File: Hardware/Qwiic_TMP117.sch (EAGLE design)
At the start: 26 parts, among them J1 PTH, U1 TMP117

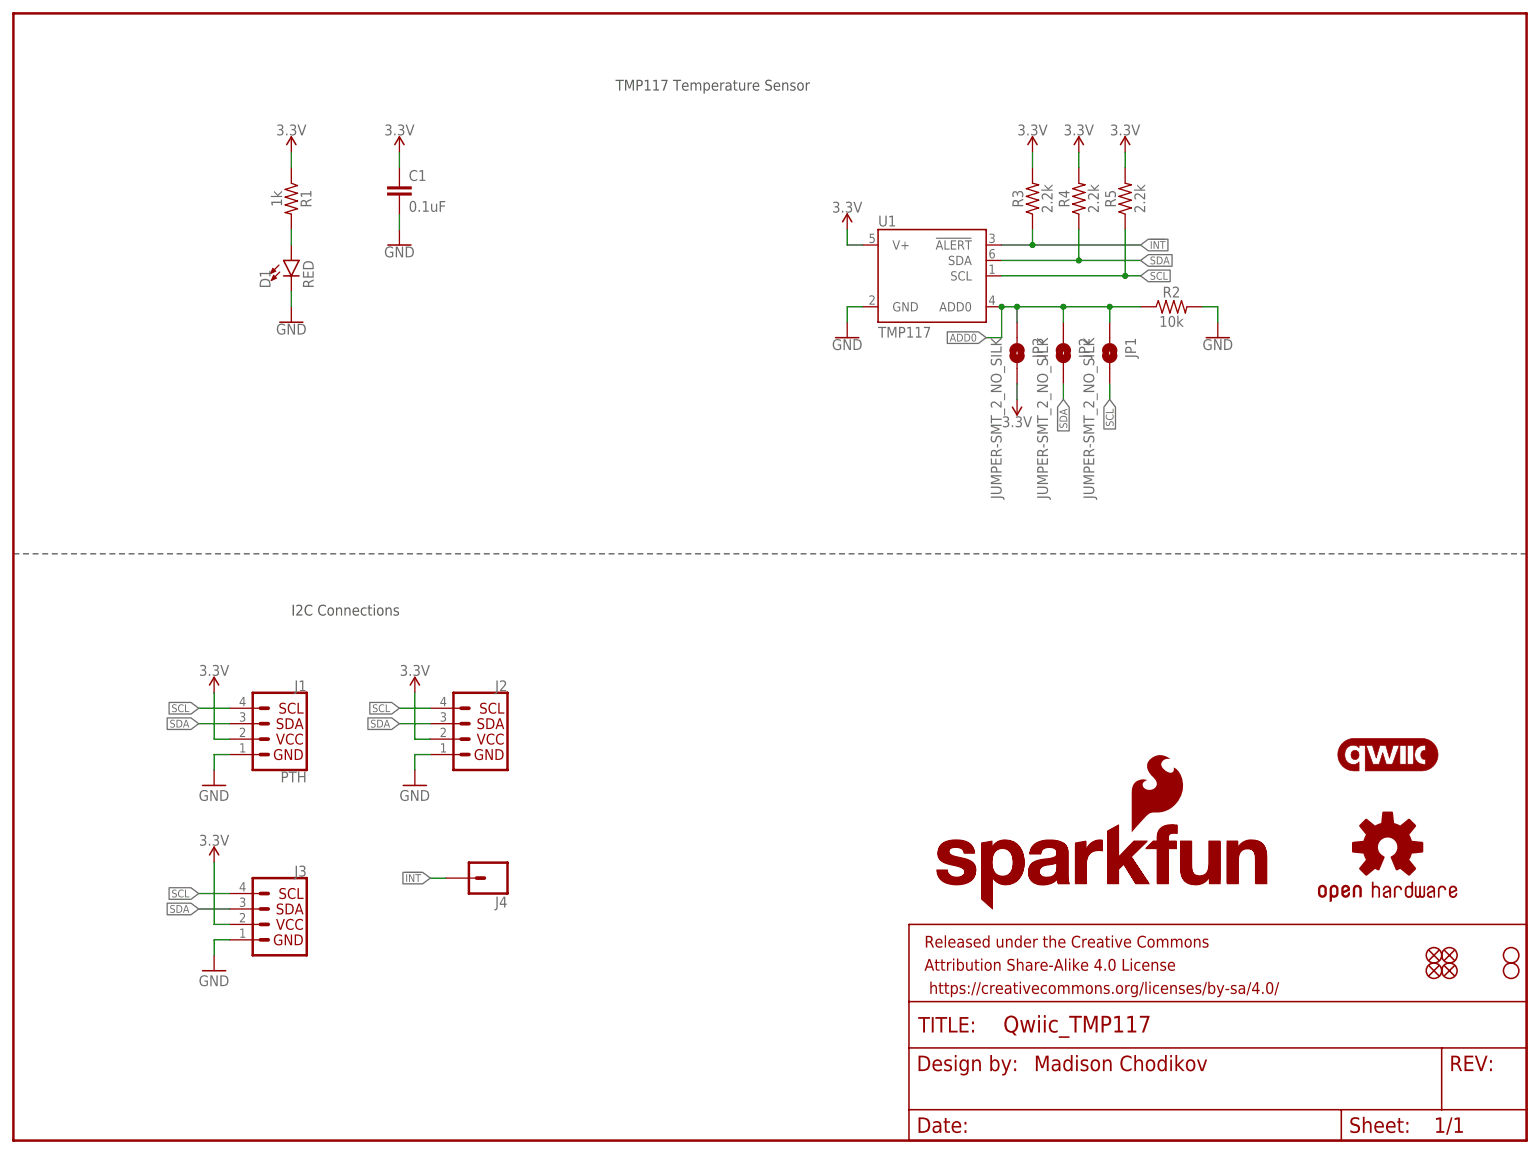
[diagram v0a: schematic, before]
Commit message: Updated Schematic and Boar
Fixed the board with the polygon and added a table to the schematic describing the pin addresses for ADD0
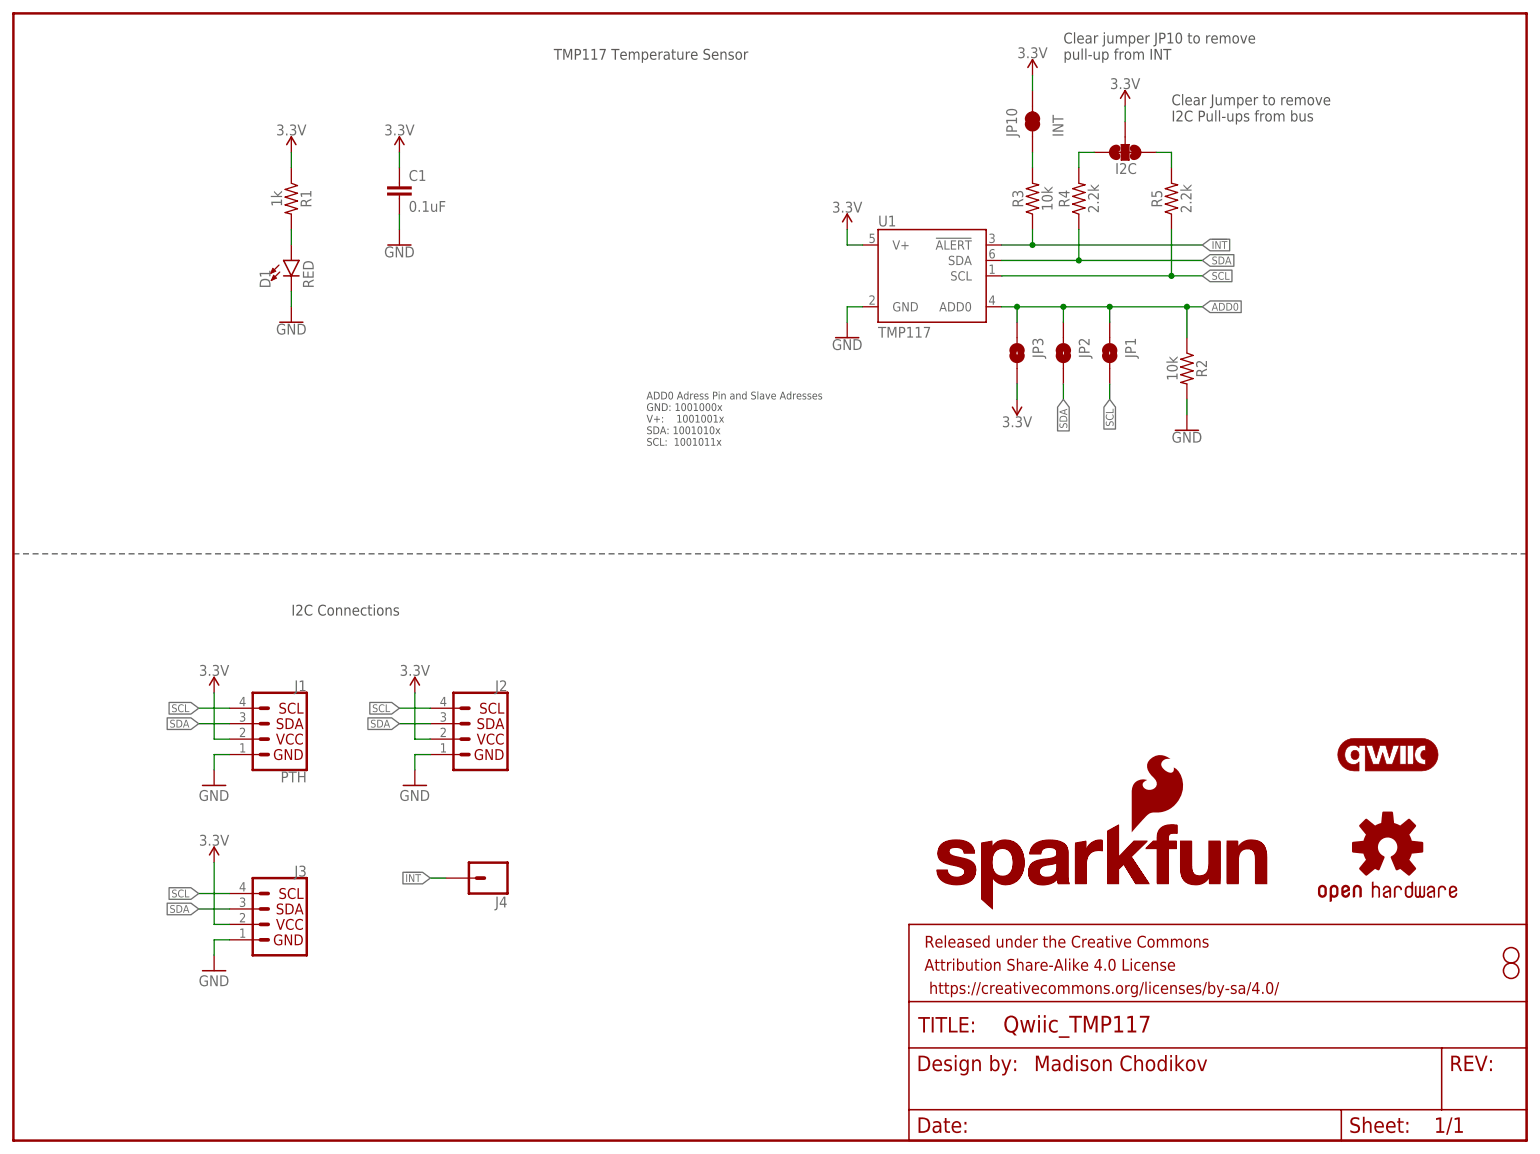
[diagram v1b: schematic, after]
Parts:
- removed JP4, JP5, JP6, JP7: FIDUCIALUFIDUCIAL, SparkFun:FIDUCIALUFIDUCIAL
- added I2C: JUMPER-SMT_3_2-NC_TRACE_SILK, SparkFun-Jumpers:JUMPER-SMT_3_2-NC_TRACE_SILK
- added JP10: INT, SparkFun-Passives:JUMPER-PAD-2-NC_BY_TRACE
- R3: value 2.2k -> 10k; device SparkFun-Resistors:2.2KOHM-0603-1/10W-1% -> SparkFun-Resistors:10KOHM-0603-1/10W-1%
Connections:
- new net N$2: I2C.1, R5.2
- new net N$3: I2C.3, R4.2
- new net N$4: JP10.1, R3.2
- net 3.3V: now also I2C.2, JP10.2; no longer R3.2, R4.2, R5.2
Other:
- note added: "ADD0 Adress Pin and Slave Adresses GND: 1001000x V+: 1001001x SDA: 1001010x SCL: 1001011x"
- note added: "Clear Jumper to remove I2C Pull-ups from bus"
- note added: "Clear jumper JP10 to remove pull-up from INT"
- moved on the sheet: R2, R5

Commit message: Updated PCB
Fixed the board to meet the specifications for the data sheet's PCB considerations
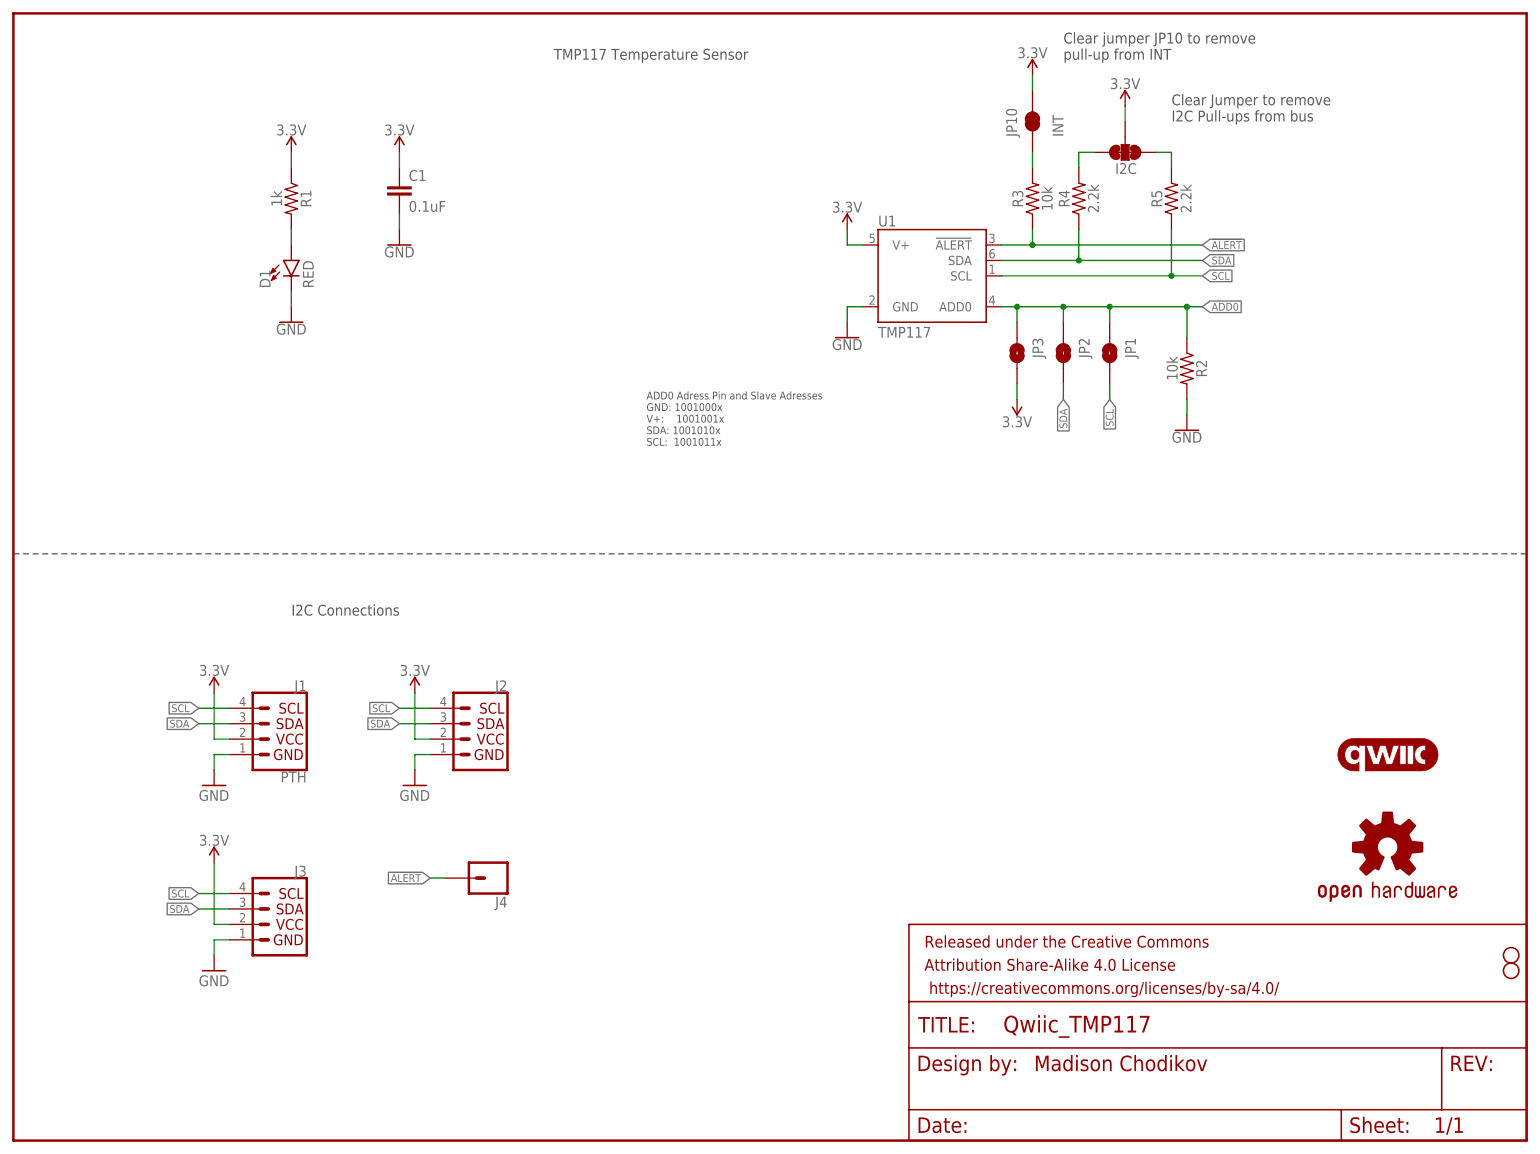
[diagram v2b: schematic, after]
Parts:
- removed U$1: SFE_LOGO_NAME.1_INCH, SparkFun-Aesthetics:SFE_LOGO_NAME.1_INCH
- removed U$2: SFE_LOGO_NAME_FLAME.1_INCH, SparkFun-Aesthetics:SFE_LOGO_NAME_FLAME.1_INCH
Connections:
- net !INT renamed !ALERT
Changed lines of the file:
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@@
 <part name="J4" library="SparkFun-Connectors" deviceset="CONN_01" device="PTH_NO_SILK_YES_STOP"/>
 <part name="SUPPLY2" library="SparkFun-PowerSymbols" library_urn="urn:adsk.eagle:library:530" deviceset="3.3V" device=""/>
-<part name="U$2" library="SparkFun-Aesthetics" deviceset="SFE_LOGO_NAME_FLAME" device=".1_INCH"/>
 <part name="LOGO1" library="SparkFun-Aesthetics" deviceset="OSHW-LOGO" device="MINI"/>
 <part name="SUPPLY7" library="SparkFun-PowerSymbols" deviceset="3.3V" device=""/>
@@
 <part name="JP8" library="SparkFun" deviceset="STAND-OFF" device=""/>
 <part name="JP9" library="SparkFun" deviceset="STAND-OFF" device=""/>
-<part name="U$1" library="SparkFun-Aesthetics" deviceset="SFE_LOGO_NAME" device=".1_INCH"/>
 <part name="U$3" library="SparkFun-Aesthetics" deviceset="QWIIC_LOGO" device="_4MM"/>
 <part name="I2C" library="SparkFun-Jumpers" library_urn="urn:adsk.eagle:library:528" deviceset="JUMPER-SMT_3_2-NC_TRACE" device="_SILK" package3d_urn="urn:adsk.eagle:package:39289/1" value=""/>
@@
 <attribute name="VALUE" x="165.1" y="119.126" size="1.778" layer="96" rot="R180" align="bottom-center"/>
 </instance>
-<instance part="U$2" gate="G$1" x="151.13" y="37.592" smashed="yes"/>
 <instance part="LOGO1" gate="G$1" x="226.06" y="48.26" smashed="yes"/>
 <instance part="SUPPLY7" gate="G$1" x="66.04" y="73.66" smashed="yes">
@@
 <instance part="JP8" gate="G$1" x="246.38" y="30.48" smashed="yes"/>
 <instance part="JP9" gate="G$1" x="246.38" y="27.94" smashed="yes"/>
-<instance part="U$1" gate="G$1" x="149.86" y="38.1" smashed="yes"/>
 <instance part="U$3" gate="G$1" x="226.06" y="63.5" smashed="yes"/>
 <instance part="I2C" gate="G$1" x="182.88" y="162.56" smashed="yes" rot="R270">
@@
 </segment>
 </net>
-<net name="!INT" class="0">
+<net name="!ALERT" class="0">
 <segment>
 <pinref part="J4" gate="G$1" pin="1"/>
@@
 <pinref part="R3" gate="G$1" pin="1"/>
 <wire x1="162.56" y1="147.32" x2="167.64" y2="147.32" width="0.1524" layer="91"/>
-<label x="195.58" y="147.32" size="1.27" layer="95" xref="yes"/>
 <wire x1="167.64" y1="147.32" x2="195.58" y2="147.32" width="0.1524" layer="91"/>
 <wire x1="167.64" y1="149.86" x2="167.64" y2="147.32" width="0.1524" layer="91"/>
 <junction x="167.64" y="147.32"/>
-</segment>
-</net>
+<label x="195.58" y="147.32" size="1.27" layer="95" xref="yes"/>
+</segment>
+</net>

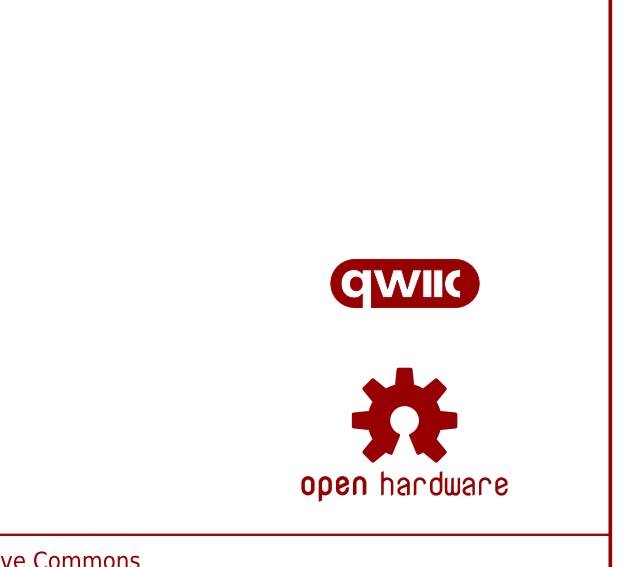
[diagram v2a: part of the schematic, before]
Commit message: Updated Board
Fixed wiring and polygons
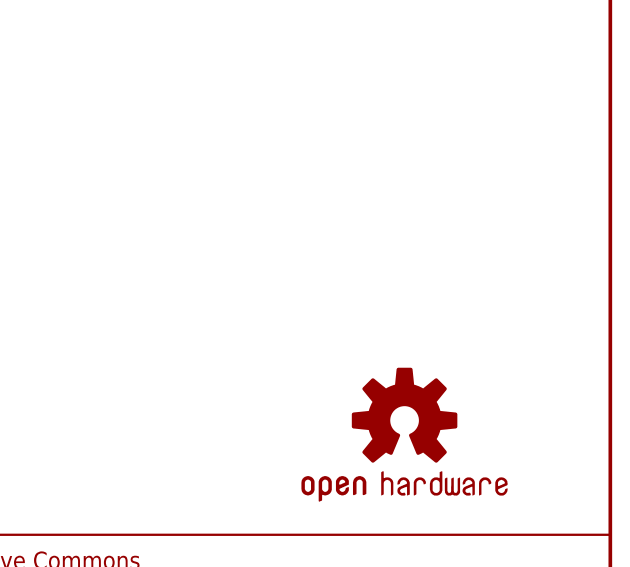
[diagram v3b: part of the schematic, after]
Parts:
- removed U$3: QWIIC_LOGO_4MM, SparkFun-Aesthetics:QWIIC_LOGO_4MM
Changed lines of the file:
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@@
 <part name="JP8" library="SparkFun" deviceset="STAND-OFF" device=""/>
 <part name="JP9" library="SparkFun" deviceset="STAND-OFF" device=""/>
-<part name="U$3" library="SparkFun-Aesthetics" deviceset="QWIIC_LOGO" device="_4MM"/>
 <part name="I2C" library="SparkFun-Jumpers" library_urn="urn:adsk.eagle:library:528" deviceset="JUMPER-SMT_3_2-NC_TRACE" device="_SILK" package3d_urn="urn:adsk.eagle:package:39289/1" value=""/>
 <part name="JP10" library="SparkFun-Passives" deviceset="JUMPER-PAD-2-NC_BY_TRACE" device="" value="INT"/>
@@
 <instance part="JP8" gate="G$1" x="246.38" y="30.48" smashed="yes"/>
 <instance part="JP9" gate="G$1" x="246.38" y="27.94" smashed="yes"/>
-<instance part="U$3" gate="G$1" x="226.06" y="63.5" smashed="yes"/>
 <instance part="I2C" gate="G$1" x="182.88" y="162.56" smashed="yes" rot="R270">
 <attribute name="NAME" x="181.229" y="159.004" size="1.778" layer="95" font="vector"/>

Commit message: Final Design
Final updated board with the production panelized board and Gerber files
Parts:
- removed U1: TMP117, my-library:TMP117
- added U2: TMP117, TMP117:TMP117
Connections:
- removed net !ALERT: J4.1, R3.1, U1.!ALERT
- new net !INT: J4.1, R3.1, U2.!INT
- net 3.3V: now also U2.V+; no longer U1.V+
- net ADD0: now also U2.ADD0; no longer U1.ADD0
- net GND: now also U2.GND; no longer U1.GND
- net SCL: now also U2.SCL; no longer U1.SCL
- net SDA: now also U2.SDA; no longer U1.SDA
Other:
- note added: "ADD0 Adress Pin and Slave Adresses GND: 1001000x V+: 1001001x SDA: 1001010x SCL: 1001011x x represents the read-write bit"
- note removed: "ADD0 Adress Pin and Slave Adresses GND: 1001000x V+: 1001001x SDA: 1001010x SCL: 1001011x"
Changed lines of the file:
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@@
 <part name="GND5" library="SparkFun" deviceset="GND" device=""/>
 <part name="GND6" library="SparkFun" deviceset="GND" device=""/>
-<part name="U1" library="my-library" deviceset="TMP117" device=""/>
 <part name="JP1" library="SparkFun-Jumpers" library_urn="urn:adsk.eagle:library:528" deviceset="JUMPER-SMT_2_NO" device="_SILK" package3d_urn="urn:adsk.eagle:package:39279/1" value=""/>
 <part name="SUPPLY5" library="SparkFun-PowerSymbols" library_urn="urn:adsk.eagle:library:530" deviceset="3.3V" device=""/>
@@
 <part name="I2C" library="SparkFun-Jumpers" library_urn="urn:adsk.eagle:library:528" deviceset="JUMPER-SMT_3_2-NC_TRACE" device="_SILK" package3d_urn="urn:adsk.eagle:package:39289/1" value=""/>
 <part name="JP10" library="SparkFun-Passives" deviceset="JUMPER-PAD-2-NC_BY_TRACE" device="" value="INT"/>
+<part name="U2" library="TMP117" deviceset="TMP117" device=""/>
 </parts>
 <sheets>
@@
 V+:    1001001x
 SDA: 1001010x
-SCL:  1001011x</text>
+SCL:  1001011x
+x represents the read-write bit</text>
 </plain>
 <instances>
@@
 <attribute name="VALUE" x="30.48" y="25.4" size="1.778" layer="96"/>
 </instance>
-<instance part="U1" gate="G$1" x="149.86" y="142.24" smashed="yes">
-<attribute name="NAME" x="142.24" y="150.368" size="1.778" layer="95"/>
-<attribute name="VALUE" x="142.24" y="132.08" size="1.778" layer="96"/>
-</instance>
 <instance part="JP1" gate="G$1" x="180.34" y="129.54" smashed="yes" rot="R270">
 <attribute name="NAME" x="182.88" y="132.08" size="1.778" layer="95" font="vector" rot="R270"/>
@@
 <attribute name="VALUE" x="172.72" y="165.1" size="1.778" layer="96" rot="R90"/>
 </instance>
+<instance part="U2" gate="G$1" x="149.86" y="142.24" smashed="yes">
+<attribute name="NAME" x="142.24" y="150.368" size="1.778" layer="95"/>
+<attribute name="VALUE" x="137.16" y="132.08" size="1.778" layer="96"/>
+</instance>
 </instances>
 <busses>
@@
 <segment>
 <pinref part="GND2" gate="1" pin="GND"/>
-<pinref part="U1" gate="G$1" pin="GND"/>
 <wire x1="137.16" y1="134.62" x2="137.16" y2="137.16" width="0.1524" layer="91"/>
 <wire x1="137.16" y1="137.16" x2="139.7" y2="137.16" width="0.1524" layer="91"/>
+<pinref part="U2" gate="G$1" pin="GND"/>
 </segment>
 <segment>
@@
 <pinref part="SUPPLY6" gate="G$1" pin="3.3V"/>
 <wire x1="137.16" y1="149.86" x2="137.16" y2="147.32" width="0.1524" layer="91"/>
-<pinref part="U1" gate="G$1" pin="V+"/>
 <wire x1="137.16" y1="147.32" x2="139.7" y2="147.32" width="0.1524" layer="91"/>
+<pinref part="U2" gate="G$1" pin="V+"/>
 </segment>
 <segment>
@@
 </segment>
 <segment>
-<pinref part="U1" gate="G$1" pin="SDA"/>
 <pinref part="R4" gate="G$1" pin="1"/>
 <wire x1="175.26" y1="144.78" x2="162.56" y2="144.78" width="0.1524" layer="91"/>
@@
 <junction x="175.26" y="144.78"/>
 <label x="195.58" y="144.78" size="1.27" layer="95" xref="yes"/>
+<pinref part="U2" gate="G$1" pin="SDA"/>
 </segment>
 <segment>
@@
 </segment>
 <segment>
-<pinref part="U1" gate="G$1" pin="SCL"/>
 <pinref part="R5" gate="G$1" pin="1"/>
 <wire x1="190.5" y1="142.24" x2="162.56" y2="142.24" width="0.1524" layer="91"/>
@@
 <junction x="190.5" y="142.24"/>
 <label x="195.58" y="142.24" size="1.27" layer="95" xref="yes"/>
+<pinref part="U2" gate="G$1" pin="SCL"/>
 </segment>
 <segment>
@@
 </segment>
 </net>
-<net name="!ALERT" class="0">
+<net name="!INT" class="0">
 <segment>
 <pinref part="J4" gate="G$1" pin="1"/>
@@
 </segment>
 <segment>
-<pinref part="U1" gate="G$1" pin="!ALERT"/>
 <pinref part="R3" gate="G$1" pin="1"/>
 <wire x1="162.56" y1="147.32" x2="167.64" y2="147.32" width="0.1524" layer="91"/>
 <wire x1="167.64" y1="147.32" x2="195.58" y2="147.32" width="0.1524" layer="91"/>
+<label x="195.58" y="147.32" size="1.27" layer="95" xref="yes"/>
+<pinref part="U2" gate="G$1" pin="!INT"/>
 <wire x1="167.64" y1="149.86" x2="167.64" y2="147.32" width="0.1524" layer="91"/>
 <junction x="167.64" y="147.32"/>
-<label x="195.58" y="147.32" size="1.27" layer="95" xref="yes"/>
 </segment>
 </net>
@@
 <net name="ADD0" class="0">
 <segment>
-<pinref part="U1" gate="G$1" pin="ADD0"/>
 <wire x1="162.56" y1="137.16" x2="165.1" y2="137.16" width="0.1524" layer="91"/>
 <pinref part="JP3" gate="G$1" pin="1"/>
@@
 <junction x="193.04" y="137.16"/>
 <label x="195.58" y="137.16" size="1.27" layer="95" xref="yes"/>
-</segment>
-</net>
+<pinref part="U2" gate="G$1" pin="ADD0"/>
+</segment>
+</net>
